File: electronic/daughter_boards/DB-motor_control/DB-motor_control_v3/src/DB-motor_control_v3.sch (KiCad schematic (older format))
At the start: 14 parts, among them P1 CONN_01X19, P2 CONN_01X08, P3 CONN_01X08, P4 CONN_01X08, P5 CONN_01X04, P6 CONN_01X15, P7 CONN_01X15, Q1 2N2222

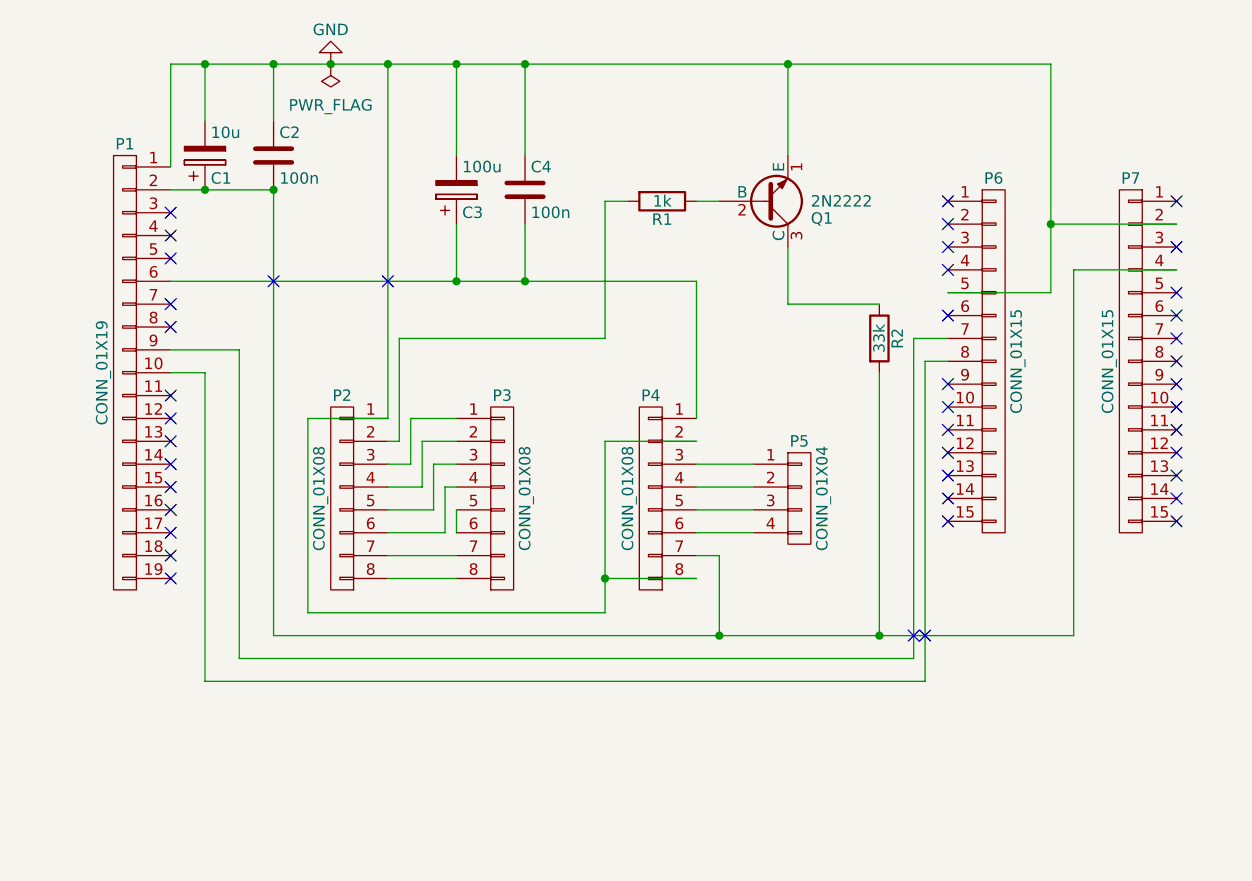
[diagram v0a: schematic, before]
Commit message: adding motor_control_v3 and trs_tgc_v2
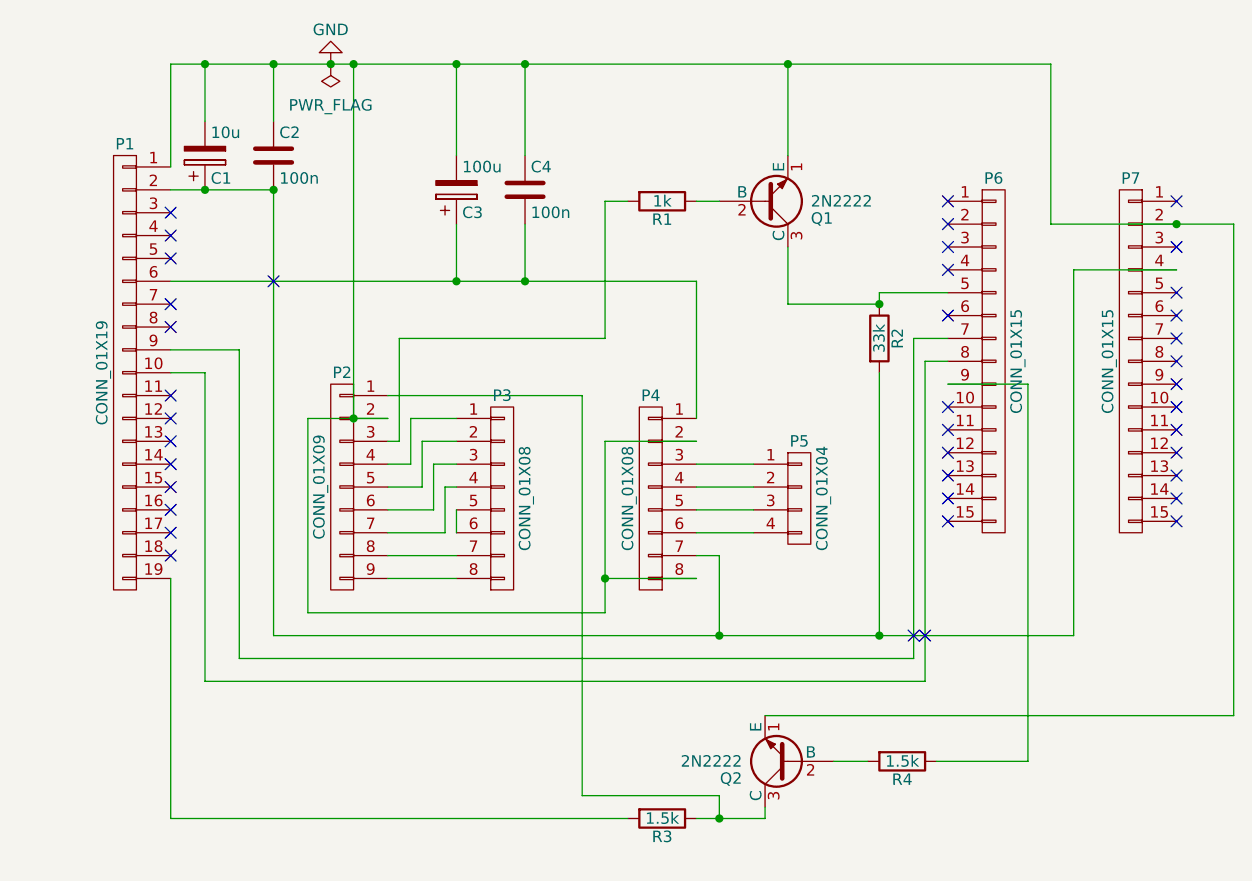
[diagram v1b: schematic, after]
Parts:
- removed P2: CONN_01X08, Echopen:Pin_Header_Straight_1x08, symbol CONN_01X08
- added P2: CONN_01X09, symbol CONN_01X09
- added Q2: 2N2222, Echopen:TO-18_TH_common, symbol 2N2222
- added R3, R4: 1.5k, Echopen:Resistor_TH_common, symbol R
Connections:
- net GND: now also P2.2 (P2), Q2.1 (E); no longer P6.5 (P5)
- net at P1.19 (P19): now also R3.2
- net at R1.2: now also P2.3 (P3)
- net at P3.1 (P1): now also P2.4 (P4)
- net at P3.2 (P2): now also P2.5 (P5)
- net at P3.3 (P3): now also P2.6 (P6)
- net at P3.4 (P4): now also P2.7 (P7)
- net at P3.7 (P7): now also P2.8 (P8)
- net at P3.8 (P8): now also P2.9 (P9)
- net at P6.9 (P9): now also R4.1
- net at Q1.3 (C), R2.1: now also P6.5 (P5)
- new net: Q2.2 (B), R4.2
- new net: P2.1 (P1), Q2.3 (C), R3.1
- no-connect marks 43 -> 40
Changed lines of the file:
@@
 Connection ~ 3850 1900
-$Comp
-L CONN_01X08 P2
-U 1 1 585A77FB
-P 4150 3800
-F 0 "P2" H 4150 4250 50  0000 C CNN
-F 1 "CONN_01X08" V 4250 3800 50  0000 C CNN
-F 2 "Echopen:Pin_Header_Straight_1x08" H 4150 3800 50  0001 C CNN
-F 3 "" H 4150 3800 50  0000 C CNN
-	1    4150 3800
-	-1   0    0    -1
-$EndComp
 $Comp
 L CONN_01X08 P3
@@
 	4400 3100 5300 3100
 Wire Wire Line
-	4350 3450 4350 1900
-Connection ~ 4350 1900
-Wire Wire Line
 	5700 4150 5300 4150
 Wire Wire Line
@@
 Wire Wire Line
 	4000 4300 4000 3450
-Wire Wire Line
-	4000 3450 4350 3450
 Wire Wire Line
 	3850 2450 3850 4400
@@
 	3400 2850 5700 2850
 NoConn ~ 3850 2850
-NoConn ~ 4350 2850
 NoConn ~ 3400 2550
 NoConn ~ 3400 2650
 NoConn ~ 3400 2750
 NoConn ~ 3400 2950
-NoConn ~ 3400 4150
 NoConn ~ 3400 4050
 Wire Wire Line
@@
 	-1   0    0    -1
 $EndComp
-Wire Wire Line
-	7250 1900 7250 2900
-Wire Wire Line
-	7250 2900 6800 2900
 Connection ~ 4950 1900
 Wire Wire Line
-	7800 2600 7250 2600
-Connection ~ 7250 2600
+	7250 2600 8050 2600
 Wire Wire Line
 	7800 2800 7350 2800
@@
 NoConn ~ 6800 2800
 NoConn ~ 6800 3000
-NoConn ~ 6800 3300
 NoConn ~ 6800 3400
 NoConn ~ 6800 3500
@@
 $EndComp
 Connection ~ 4100 1900
+Wire Wire Line
+	7250 1900 7250 2600
+Wire Wire Line
+	6800 2900 6500 2900
+Wire Wire Line
+	6500 2900 6500 2950
+Connection ~ 6500 2950
+$Comp
+L R R4
+U 1 1 58824A15
+P 6600 4950
+F 0 "R4" V 6680 4950 50  0000 C CNN
+F 1 "1.5k" V 6600 4950 50  0000 C CNN
+F 2 "Echopen:Resistor_TH_common" V 6530 4950 50  0001 C CNN
+F 3 "" H 6600 4950 50  0000 C CNN
+	1    6600 4950
+	0    1    1    0
+$EndComp
+$Comp
+L 2N2222 Q2
+U 1 1 58824BB0
+P 6100 4950
+F 0 "Q2" H 6300 5025 50  0000 L CNN
+F 1 "2N2222" H 6300 4950 50  0000 L CNN
+F 2 "Echopen:TO-18_TH_common" H 6300 4875 50  0001 L CIN
+F 3 "" H 6100 4950 50  0000 L CNN
+	1    6100 4950
+	-1   0    0    1
+$EndComp
+Wire Wire Line
+	6450 4950 6300 4950
+Wire Wire Line
+	6800 3300 7150 3300
+Wire Wire Line
+	7150 3300 7150 4950
+Wire Wire Line
+	7150 4950 6750 4950
+Wire Wire Line
+	3400 4150 3400 5200
+Wire Wire Line
+	3400 5200 5400 5200
+$Comp
+L R R3
+U 1 1 588250BD
+P 5550 5200
+F 0 "R3" V 5630 5200 50  0000 C CNN
+F 1 "1.5k" V 5550 5200 50  0000 C CNN
+F 2 "Echopen:Resistor_TH_common" V 5480 5200 50  0001 C CNN
+F 3 "" H 5550 5200 50  0000 C CNN
+	1    5550 5200
+	0    1    1    0
+$EndComp
+Wire Wire Line
+	5700 5200 6000 5200
+Wire Wire Line
+	6000 5200 6000 5150
+Wire Wire Line
+	6000 4750 8050 4750
+Wire Wire Line
+	8050 4750 8050 2600
+Connection ~ 7800 2600
+$Comp
+L CONN_01X09 P2
+U 1 1 58825882
+P 4150 3750
+F 0 "P2" H 4150 4250 50  0000 C CNN
+F 1 "CONN_01X09" V 4250 3750 50  0000 C CNN
+F 2 "" H 4150 3750 50  0001 C CNN
+F 3 "" H 4150 3750 50  0000 C CNN
+	1    4150 3750
+	-1   0    0    -1
+$EndComp
+Wire Wire Line
+	4000 3450 4350 3450
+Wire Wire Line
+	4200 3450 4200 1900
+Connection ~ 4200 1900
+Connection ~ 4200 3450
+Wire Wire Line
+	4350 3350 5200 3350
+Wire Wire Line
+	5200 3350 5200 5100
+Wire Wire Line
+	5200 5100 5800 5100
+Wire Wire Line
+	5800 5100 5800 5200
+Connection ~ 5800 5200
 $EndSCHEMATC

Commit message: sorting codes
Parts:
- R1: value 1k -> 680
- R2: value 33k -> 1.5k
- R4: value 1.5k -> 680
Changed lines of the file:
@@
 P 5550 2500
 F 0 "R1" V 5630 2500 50  0000 C CNN
-F 1 "1k" V 5550 2500 50  0000 C CNN
+F 1 "680" V 5550 2500 50  0000 C CNN
 F 2 "Echopen:Resistor_TH_common" V 5480 2500 50  0001 C CNN
 F 3 "" H 5550 2500 50  0000 C CNN
@@
 P 6500 3100
 F 0 "R2" V 6580 3100 50  0000 C CNN
-F 1 "33k" V 6500 3100 50  0000 C CNN
+F 1 "1.5k" V 6500 3100 50  0000 C CNN
 F 2 "Echopen:Resistor_TH_common" V 6430 3100 50  0001 C CNN
 F 3 "" H 6500 3100 50  0000 C CNN
@@
 P 6600 4950
 F 0 "R4" V 6680 4950 50  0000 C CNN
-F 1 "1.5k" V 6600 4950 50  0000 C CNN
+F 1 "680" V 6600 4950 50  0000 C CNN
 F 2 "Echopen:Resistor_TH_common" V 6530 4950 50  0001 C CNN
 F 3 "" H 6600 4950 50  0000 C CNN

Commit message: correct MDL pulser and update DB motor control
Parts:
- P2: footprint (none) -> Echopen:Socket_1x09
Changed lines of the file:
@@
 F 0 "P2" H 4150 4250 50  0000 C CNN
 F 1 "CONN_01X09" V 4250 3750 50  0000 C CNN
-F 2 "" H 4150 3750 50  0001 C CNN
+F 2 "Echopen:Socket_1x09" H 4150 3750 50  0001 C CNN
 F 3 "" H 4150 3750 50  0000 C CNN
 	1    4150 3750

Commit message: adding motor_control_v3 documentation
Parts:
- added C5: 47n, Echopen:C_small_TH_echopen, symbol C
- added C6: 10u, Echopen:CP_small_TH_echopen, symbol CP
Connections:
- net GND: now also C5.2, C6.2
- net at P1.11 (P11): now also P2.1 (P1), Q2.3 (C), R3.1
- net at P1.19 (P19), R3.2: now also P4.7 (P7), C5.1, C6.1
- net at C1.1, C2.2, P1.2 (P2)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: no longer P4.7 (P7)
- no-connect marks 40 -> 39
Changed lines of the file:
@@
 	3400 2350 3400 1900
 Wire Wire Line
-	3400 1900 7250 1900
+	2750 1900 7250 1900
 $Comp
 L GND #PWR01
@@
 	3850 4400 7350 4400
 Wire Wire Line
-	5800 4400 5800 4050
-Wire Wire Line
 	5800 4050 5700 4050
 $Comp
@@
 Wire Wire Line
 	7350 2800 7350 4400
-Connection ~ 5800 4400
 Wire Wire Line
 	3400 2450 3850 2450
@@
 NoConn ~ 6700 4400
 NoConn ~ 3400 3050
-NoConn ~ 3400 3350
 NoConn ~ 3400 3450
 NoConn ~ 3400 3550
@@
 Connection ~ 4200 3450
 Wire Wire Line
-	4350 3350 5200 3350
+	3400 3350 5200 3350
 Wire Wire Line
 	5200 3350 5200 5100
@@
 	5800 5100 5800 5200
 Connection ~ 5800 5200
+$Comp
+L CP C6
+U 1 1 58ECF1A9
+P 3250 5200
+F 0 "C6" H 3275 5300 50  0000 L CNN
+F 1 "10u" H 3275 5100 50  0000 L CNN
+F 2 "Echopen:CP_small_TH_echopen" H 3288 5050 50  0001 C CNN
+F 3 "" H 3250 5200 50  0001 C CNN
+	1    3250 5200
+	0    1    1    0
+$EndComp
+Wire Wire Line
+	2750 1900 2750 5200
+Wire Wire Line
+	2750 5200 3100 5200
+Connection ~ 3400 1900
+$Comp
+L C C5
+U 1 1 58ECF3F6
+P 3100 4900
+F 0 "C5" H 3125 5000 50  0000 L CNN
+F 1 "47n" H 3125 4800 50  0000 L CNN
+F 2 "Echopen:C_small_TH_echopen" H 3138 4750 50  0001 C CNN
+F 3 "" H 3100 4900 50  0001 C CNN
+	1    3100 4900
+	0    1    1    0
+$EndComp
+Wire Wire Line
+	3250 4900 3400 4900
+Connection ~ 3400 4900
+Wire Wire Line
+	2950 4900 2750 4900
+Connection ~ 2750 4900
+Wire Wire Line
+	5800 4050 5800 4800
+Wire Wire Line
+	5800 4800 4550 4800
+Wire Wire Line
+	4550 4800 4550 5200
+Connection ~ 4550 5200
+Connection ~ 4350 3350
 $EndSCHEMATC
